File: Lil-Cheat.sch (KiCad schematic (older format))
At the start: 129 parts, among them J1 USB2_C_Receptacle, SW1 SW_Push, U1 ATmega32U2-AU, U2 SRV05-4, Y1 16MHz

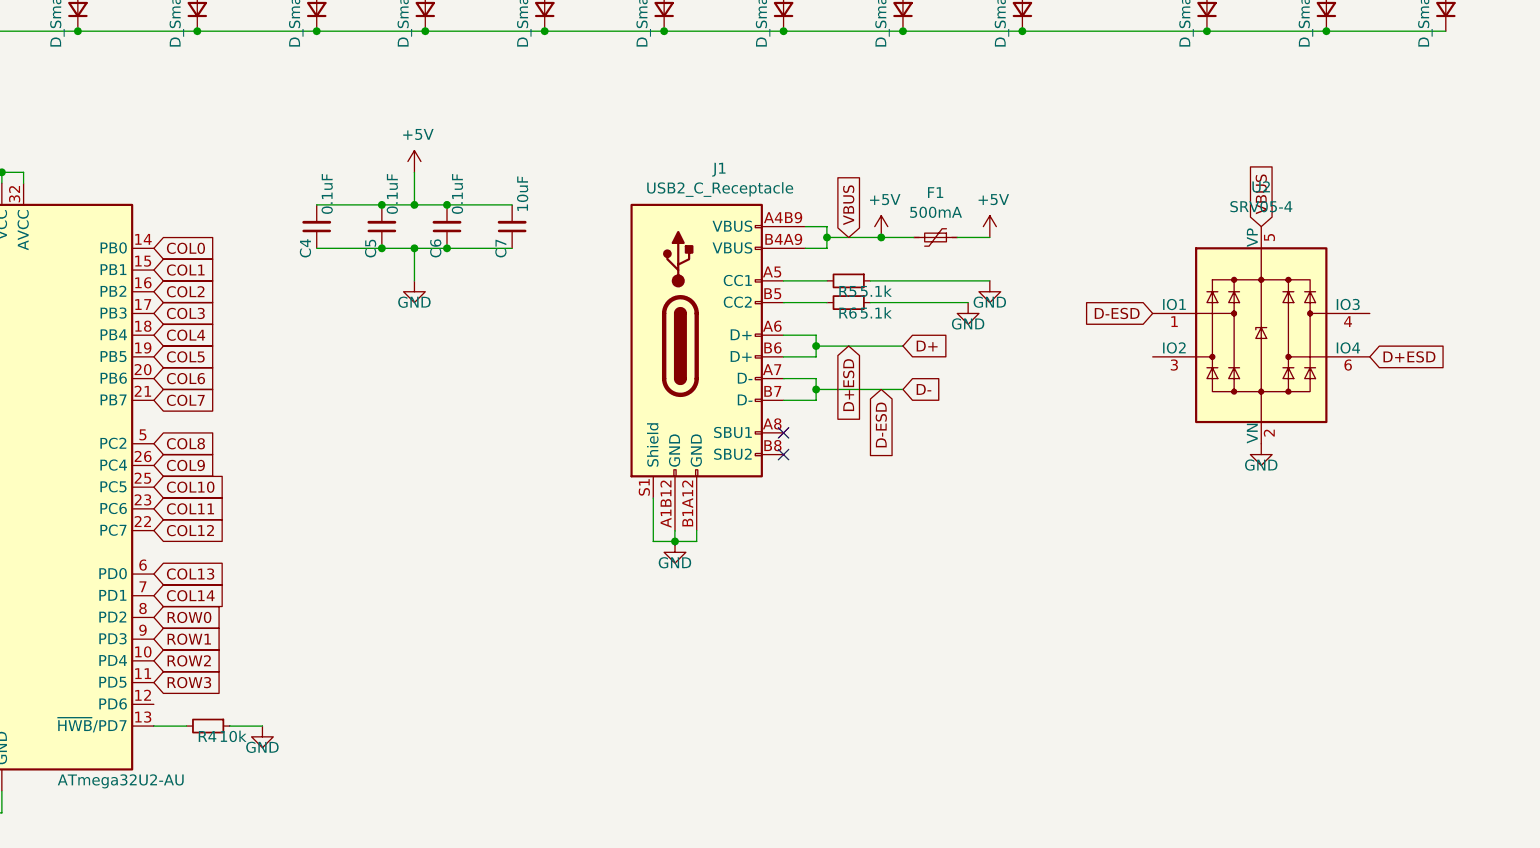
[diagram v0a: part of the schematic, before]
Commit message: swapped to daughterboard
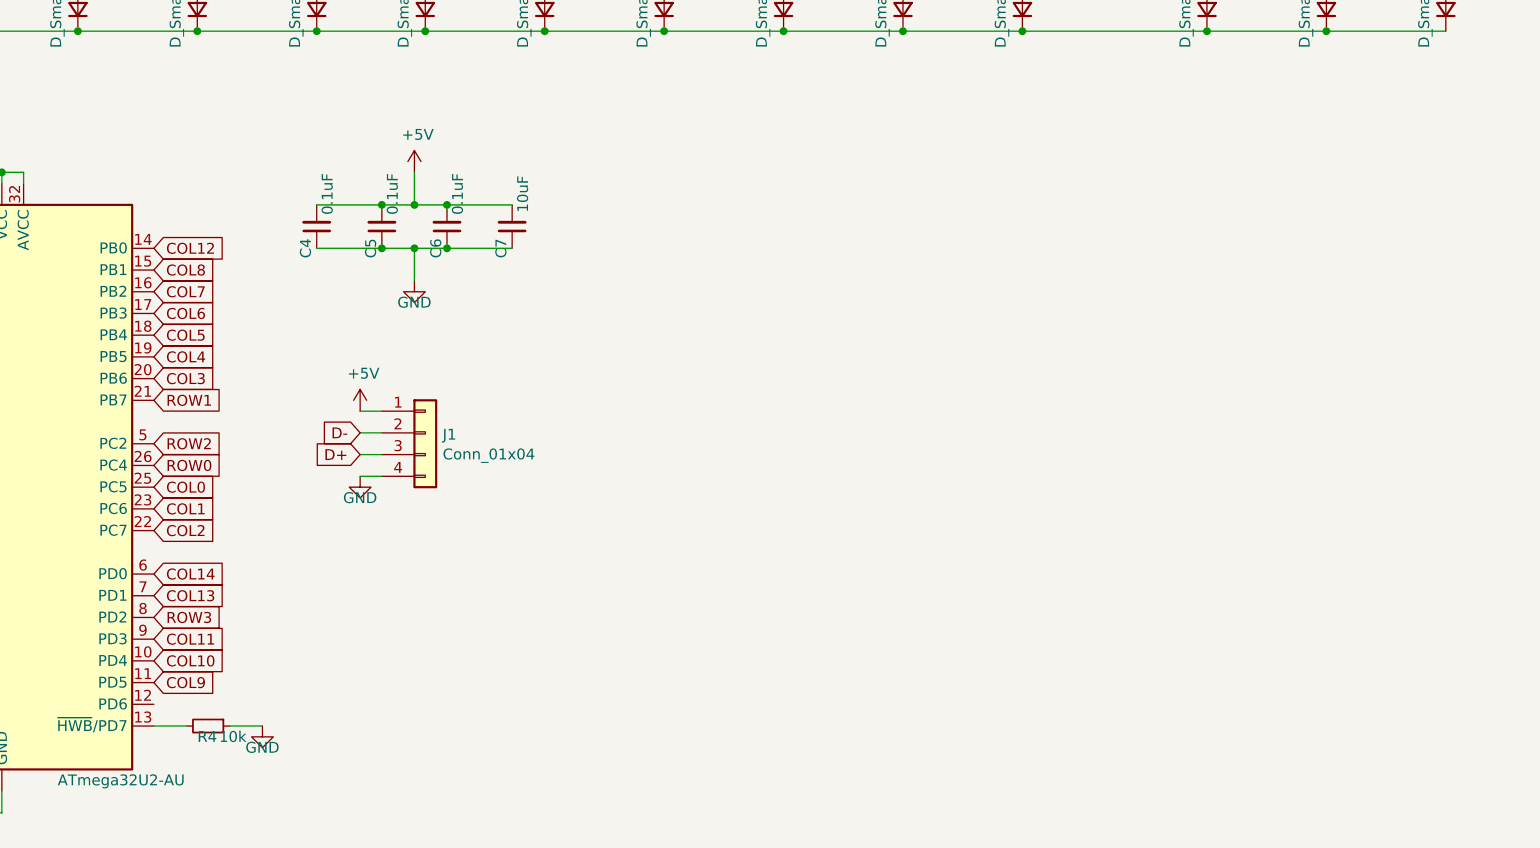
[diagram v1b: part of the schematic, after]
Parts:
- removed F1: 500mA, Fuse:Fuse_1206_3216Metric, symbol Device:Polyfuse_Small
- removed J1: USB2_C_Receptacle, usb-type-c:Mid_Mount-USB_C, symbol usb-type-c:USB2_C_Receptacle
- removed R5, R6: 5.1k, Resistor_SMD:R_0805_2012Metric, symbol Device:R_Small
- removed U2: SRV05-4, Package_TO_SOT_SMD:SOT-23-6, symbol Power_Protection:SRV05-4
- added J1: Conn_01x04, Connector_JST:JST_SUR_SM04B-SURS-TF_1x04-1MP_P0.80mm_Horizontal, symbol Connector_Generic:Conn_01x04
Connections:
- net +5V: now also J1.1 (Pin_1)
- net COL0: now also U1.25 (PC5); no longer U1.14 (PB0)
- net COL1: now also U1.23 (PC6); no longer U1.15 (PB1)
- net COL10: now also U1.10 (PD4); no longer U1.25 (PC5)
- net COL11: now also U1.9 (PD3); no longer U1.23 (PC6)
- net COL12: now also U1.14 (PB0); no longer U1.22 (PC7)
- net COL13: now also U1.7 (PD1); no longer U1.6 (PD0)
- net COL14: now also U1.6 (PD0); no longer U1.7 (PD1)
- net COL2: now also U1.22 (PC7); no longer U1.16 (PB2)
- net COL3: now also U1.20 (PB6); no longer U1.17 (PB3)
- net COL4: now also U1.19 (PB5); no longer U1.18 (PB4)
- net COL5: now also U1.18 (PB4); no longer U1.19 (PB5)
- net COL6: now also U1.17 (PB3); no longer U1.20 (PB6)
- net COL7: now also U1.16 (PB2); no longer U1.21 (PB7)
- net COL8: now also U1.15 (PB1); no longer U1.5 (PC2)
- net COL9: now also U1.11 (PD5); no longer U1.26 (PC4)
- net D+: now also J1.3 (Pin_3)
- net D-: now also J1.2 (Pin_2)
- net GND: now also J1.4 (Pin_4)
- net ROW0: now also U1.26 (PC4); no longer U1.8 (PD2)
- net ROW1: now also U1.21 (PB7); no longer U1.9 (PD3)
- net ROW2: now also U1.5 (PC2); no longer U1.10 (PD4)
- net ROW3: now also U1.8 (PD2); no longer U1.11 (PD5)
- no-connect marks 2 -> 0
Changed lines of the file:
@@
 Wire Wire Line
 	4050 7150 4200 7150
+Text GLabel 3700 6050 2    50   Input ~ 0
+COL0
+Text GLabel 3700 6150 2    50   Input ~ 0
+COL1
+Text GLabel 3700 6250 2    50   Input ~ 0
+COL2
+Text GLabel 3700 5550 2    50   Input ~ 0
+COL3
+Text GLabel 3700 5450 2    50   Input ~ 0
+COL4
+Text GLabel 3700 5350 2    50   Input ~ 0
+COL5
+Text GLabel 3700 5250 2    50   Input ~ 0
+COL6
+Text GLabel 3700 5150 2    50   Input ~ 0
+COL7
+Text GLabel 3700 5050 2    50   Input ~ 0
+COL8
+Text GLabel 3700 6950 2    50   Input ~ 0
+COL9
+Text GLabel 3700 6850 2    50   Input ~ 0
+COL10
+Text GLabel 3700 6750 2    50   Input ~ 0
+COL11
 Text GLabel 3700 4950 2    50   Input ~ 0
-COL0
-Text GLabel 3700 5050 2    50   Input ~ 0
-COL1
-Text GLabel 3700 5150 2    50   Input ~ 0
-COL2
-Text GLabel 3700 5250 2    50   Input ~ 0
-COL3
-Text GLabel 3700 5350 2    50   Input ~ 0
-COL4
-Text GLabel 3700 5450 2    50   Input ~ 0
-COL5
-Text GLabel 3700 5550 2    50   Input ~ 0
-COL6
+COL12
+Text GLabel 3700 6550 2    50   Input ~ 0
+COL13
+Text GLabel 3700 6450 2    50   Input ~ 0
+COL14
+Text GLabel 3700 5950 2    50   Input ~ 0
+ROW0
 Text GLabel 3700 5650 2    50   Input ~ 0
-COL7
+ROW1
 Text GLabel 3700 5850 2    50   Input ~ 0
-COL8
-Text GLabel 3700 5950 2    50   Input ~ 0
-COL9
-Text GLabel 3700 6050 2    50   Input ~ 0
-COL10
-Text GLabel 3700 6150 2    50   Input ~ 0
-COL11
-Text GLabel 3700 6250 2    50   Input ~ 0
-COL12
-Text GLabel 3700 6450 2    50   Input ~ 0
-COL13
-Text GLabel 3700 6550 2    50   Input ~ 0
-COL14
+ROW2
 Text GLabel 3700 6650 2    50   Input ~ 0
-ROW0
-Text GLabel 3700 6750 2    50   Input ~ 0
-ROW1
-Text GLabel 3700 6850 2    50   Input ~ 0
-ROW2
-Text GLabel 3700 6950 2    50   Input ~ 0
 ROW3
 $Comp
@@
 	4900 4950 4750 4950
 $Comp
-L Power_Protection:SRV05-4 U2
-U 1 1 5FD42A2A
-P 8800 5350
-F 0 "U2" H 8800 6031 50  0000 C CNN
-F 1 "SRV05-4" H 8800 5940 50  0000 C CNN
-F 2 "Package_TO_SOT_SMD:SOT-23-6" H 9500 4900 50  0001 C CNN
-F 3 "http://www.onsemi.com/pub/Collateral/SRV05-4-D.PDF" H 8800 5350 50  0001 C CNN
-	1    8800 5350
+L power:+5V #PWR0111
+U 1 1 5FD497C3
+P 4650 5700
+F 0 "#PWR0111" H 4650 5550 50  0001 C CNN
+F 1 "+5V" H 4665 5873 50  0000 C CNN
+F 2 "" H 4650 5700 50  0001 C CNN
+F 3 "" H 4650 5700 50  0001 C CNN
+	1    4650 5700
 	1    0    0    -1
 $EndComp
-$Comp
-L Device:Polyfuse_Small F1
-U 1 1 5FD47DB5
-P 7300 4900
-F 0 "F1" V 7095 4900 50  0000 C CNN
-F 1 "500mA" V 7186 4900 50  0000 C CNN
-F 2 "Fuse:Fuse_1206_3216Metric" H 7350 4700 50  0001 L CNN
-F 3 "~" H 7300 4900 50  0001 C CNN
-	1    7300 4900
-	0    1    1    0
-$EndComp
-$Comp
-L power:+5V #PWR0110
-U 1 1 5FD48F9E
-P 7050 4900
-F 0 "#PWR0110" H 7050 4750 50  0001 C CNN
-F 1 "+5V" H 7065 5073 50  0000 C CNN
-F 2 "" H 7050 4900 50  0001 C CNN
-F 3 "" H 7050 4900 50  0001 C CNN
-	1    7050 4900
-	1    0    0    -1
-$EndComp
-$Comp
-L power:+5V #PWR0111
-U 1 1 5FD497C3
-P 7550 4900
-F 0 "#PWR0111" H 7550 4750 50  0001 C CNN
-F 1 "+5V" H 7565 5073 50  0000 C CNN
-F 2 "" H 7550 4900 50  0001 C CNN
-F 3 "" H 7550 4900 50  0001 C CNN
-	1    7550 4900
-	1    0    0    -1
-$EndComp
-$Comp
-L usb-type-c:USB2_C_Receptacle J1
-U 1 1 5FD4E20F
-P 6200 5400
-F 0 "J1" H 6307 6217 50  0000 C CNN
-F 1 "USB2_C_Receptacle" H 6307 6126 50  0000 C CNN
-F 2 "usb-type-c:Mid_Mount-USB_C" H 6400 5450 50  0001 C CNN
-F 3 " ~" H 6400 5450 50  0001 C CNN
-	1    6200 5400
-	1    0    0    -1
-$EndComp
-Wire Wire Line
-	6700 4850 6800 4850
-Wire Wire Line
-	6800 4950 6700 4950
-Text GLabel 6900 4900 1    50   Input ~ 0
-VBUS
-Wire Wire Line
-	6800 4850 6800 4900
-Wire Wire Line
-	6800 4900 7050 4900
-Connection ~ 6800 4900
-Wire Wire Line
-	6800 4900 6800 4950
-Connection ~ 7050 4900
-Wire Wire Line
-	7050 4900 7200 4900
-Wire Wire Line
-	7400 4900 7550 4900
-$Comp
-L Device:R_Small R5
-U 1 1 5FDF8EEE
-P 6900 5100
-F 0 "R5" V 6950 5050 50  0000 L CNN
-F 1 "5.1k" V 6950 5150 50  0000 L CNN
-F 2 "Resistor_SMD:R_0805_2012Metric" H 6900 5100 50  0001 C CNN
-F 3 "~" H 6900 5100 50  0001 C CNN
-	1    6900 5100
-	0    1    1    0
-$EndComp
-$Comp
-L Device:R_Small R6
-U 1 1 5FDF988D
-P 6900 5200
-F 0 "R6" V 6950 5150 50  0000 L CNN
-F 1 "5.1k" V 6950 5250 50  0000 L CNN
-F 2 "Resistor_SMD:R_0805_2012Metric" H 6900 5200 50  0001 C CNN
-F 3 "~" H 6900 5200 50  0001 C CNN
-	1    6900 5200
-	0    1    1    0
-$EndComp
-$Comp
-L power:GND #PWR0112
-U 1 1 5FDF9DE8
-P 7450 5200
-F 0 "#PWR0112" H 7450 4950 50  0001 C CNN
-F 1 "GND" H 7450 5100 50  0000 C CNN
-F 2 "" H 7450 5200 50  0001 C CNN
-F 3 "" H 7450 5200 50  0001 C CNN
-	1    7450 5200
-	1    0    0    -1
-$EndComp
-$Comp
-L power:GND #PWR0113
-U 1 1 5FDFA53C
-P 7550 5100
-F 0 "#PWR0113" H 7550 4850 50  0001 C CNN
-F 1 "GND" H 7550 5000 50  0000 C CNN
-F 2 "" H 7550 5100 50  0001 C CNN
-F 3 "" H 7550 5100 50  0001 C CNN
-	1    7550 5100
-	1    0    0    -1
-$EndComp
-Wire Wire Line
-	6600 5100 6800 5100
-Wire Wire Line
-	6600 5200 6800 5200
-Wire Wire Line
-	7000 5100 7550 5100
-Wire Wire Line
-	7000 5200 7450 5200
-NoConn ~ 6600 5800
-NoConn ~ 6600 5900
-Wire Wire Line
-	6600 5350 6750 5350
-Wire Wire Line
-	6750 5350 6750 5400
-Wire Wire Line
-	6750 5450 6600 5450
-Wire Wire Line
-	6600 5550 6750 5550
-Wire Wire Line
-	6750 5550 6750 5600
-Wire Wire Line
-	6750 5650 6600 5650
-Text GLabel 7150 5400 2    50   Input ~ 0
+Text GLabel 4650 5900 0    50   Input ~ 0
 D+
 Text GLabel 1650 5750 0    50   Input ~ 0
 D-
-Text GLabel 7150 5600 2    50   Input ~ 0
+Text GLabel 4650 5800 0    50   Input ~ 0
 D-
-Text GLabel 6900 5400 3    50   Input ~ 0
-D+ESD
-Text GLabel 7050 5600 3    50   Input ~ 0
-D-ESD
-Wire Wire Line
-	6750 5400 7150 5400
-Connection ~ 6750 5400
-Wire Wire Line
-	6750 5400 6750 5450
-Wire Wire Line
-	6750 5600 7150 5600
-Connection ~ 6750 5600
-Wire Wire Line
-	6750 5600 6750 5650
-Wire Wire Line
-	6000 6100 6000 6300
-Wire Wire Line
-	6000 6300 6100 6300
-Wire Wire Line
-	6200 6300 6200 6250
-Wire Wire Line
-	6100 6250 6100 6300
-Connection ~ 6100 6300
-Wire Wire Line
-	6100 6300 6200 6300
 $Comp
 L power:GND #PWR0114
 U 1 1 5FF03786
-P 6100 6300
-F 0 "#PWR0114" H 6100 6050 50  0001 C CNN
-F 1 "GND" H 6100 6200 50  0000 C CNN
-F 2 "" H 6100 6300 50  0001 C CNN
-F 3 "" H 6100 6300 50  0001 C CNN
-	1    6100 6300
+P 4650 6000
+F 0 "#PWR0114" H 4650 5750 50  0001 C CNN
+F 1 "GND" H 4650 5900 50  0000 C CNN
+F 2 "" H 4650 6000 50  0001 C CNN
+F 3 "" H 4650 6000 50  0001 C CNN
+	1    4650 6000
 	1    0    0    -1
 $EndComp
-$Comp
-L power:GND #PWR0115
-U 1 1 5FF03BAA
-P 8800 5850
-F 0 "#PWR0115" H 8800 5600 50  0001 C CNN
-F 1 "GND" H 8800 5750 50  0000 C CNN
-F 2 "" H 8800 5850 50  0001 C CNN
-F 3 "" H 8800 5850 50  0001 C CNN
-	1    8800 5850
-	1    0    0    -1
-$EndComp
-Text GLabel 8800 4850 1    50   Input ~ 0
-VBUS
-Text GLabel 8300 5250 0    50   Input ~ 0
-D-ESD
-Text GLabel 9300 5450 2    50   Input ~ 0
-D+ESD
 Wire Wire Line
 	1700 2000 1350 2000
@@
 	1700 2650 1350 2650
 Connection ~ 1700 2650
+Wire Wire Line
+	4750 5700 4650 5700
+Wire Wire Line
+	4750 5800 4650 5800
+Wire Wire Line
+	4750 5900 4650 5900
+Wire Wire Line
+	4750 6000 4650 6000
+$Comp
+L Connector_Generic:Conn_01x04 J1
+U 1 1 5F9747C0
+P 4950 5800
+F 0 "J1" H 5030 5792 50  0000 L CNN
+F 1 "Conn_01x04" H 5030 5701 50  0000 L CNN
+F 2 "Connector_JST:JST_SUR_SM04B-SURS-TF_1x04-1MP_P0.80mm_Horizontal" H 4950 5800 50  0001 C CNN
+F 3 "~" H 4950 5800 50  0001 C CNN
+	1    4950 5800
+	1    0    0    -1
+$EndComp
 $EndSCHEMATC
